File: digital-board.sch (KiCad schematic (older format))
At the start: 200 parts, among them IC1 ATMEGA6450-A, J1 CONN_20X2, Q1 2N3904, Q10 2N3904, Q11 2N3904, Q12 2N3904, Q13 2N3904, Q14 2N3904, Q15 2N3904, Q16 2N3904, Q2 2N3904, Q3 2N3904, Q4 2N3904, Q5 2N3904, Q6 2N3904, Q7 2N3904, Q8 2N3904, Q9 2N3904, SW15 TACT_SWITCH, SW16 TACT_SWITCH, SW17 TACT_SWITCH, SW18 TACT_SWITCH, SW19 TACT_SWITCH, SW20 TACT_SWITCH, SW21 TACT_SWITCH, SW22 TACT_SWITCH, SW23 TACT_SWITCH, U1 DG419, U10 74LVC1G32, U2 74HC4067, U3 R-78E5.0-1.0, U4 74HC4067, U5 74LS573, U6 74LS573, U7 74LVC2G04, U8 74LS573, U9 74LS573, X1 MIDI OUT, X2 MIDI IN, X3 MIDI THRU

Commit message: commit
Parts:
- removed U8, U9: 74LS573, symbol 74LS573
- added U?: 74AC273, symbol 74AC273
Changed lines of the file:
@@
 $EndComp
 $Comp
-L 74LS573 U9
-U 1 1 5458825E
-P 18600 16650
-F 0 "U9" H 18750 17250 60  0000 C CNN
-F 1 "74LS573" H 18850 16050 60  0000 C CNN
-F 2 "" H 18600 16650 60  0000 C CNN
-F 3 "" H 18600 16650 60  0000 C CNN
-	1    18600 16650
-	1    0    0    -1
-$EndComp
-$Comp
 L C_US C14
 U 1 1 54588264
@@
 LFO SYNC LED DRIVEN BY LFO OUTPUT\nLED DRIVER FROM YUSYNTH VCO\nTESTED BY BREADBOARD
 $Comp
-L 74LS573 U8
-U 1 1 545882D7
-P 16250 11350
-F 0 "U8" H 16400 11950 60  0000 C CNN
-F 1 "74LS573" H 16500 10750 60  0000 C CNN
-F 2 "" H 16250 11350 60  0000 C CNN
-F 3 "" H 16250 11350 60  0000 C CNN
-	1    16250 11350
-	1    0    0    -1
-$EndComp
-$Comp
 L C_US C13
 U 1 1 545882DD
@@
 Wire Wire Line
 	19500 20200 19750 20200
-Wire Notes Line
-	30000 2800 30000 5800
-Wire Notes Line
-	30000 5800 29550 5800
-Wire Notes Line
-	29550 5800 29550 3500
-Wire Notes Line
-	29550 3500 31600 3500
-Wire Notes Line
-	31600 3500 31600 9100
-Wire Notes Line
-	31600 9100 32300 9100
-Wire Notes Line
-	32300 9100 32300 6850
-Wire Notes Line
-	32300 6850 30150 6850
-Wire Notes Line
-	30150 6850 30150 11000
+$Comp
+L 74AC273 U?
+U 1 1 54A8D023
+P 30350 8100
+F 0 "U?" H 30000 8700 60  0000 C CNN
+F 1 "74AC273" H 30575 7500 60  0000 C CNN
+F 2 "" H 30350 8100 60  0000 C CNN
+F 3 "" H 30350 8100 60  0000 C CNN
+	1    30350 8100
+	1    0    0    -1
+$EndComp
 $EndSCHEMATC

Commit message: working on 74AC595 LED arrays
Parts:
- removed C14, C15: 0.1µ, ~, symbol C_US
- removed Q10, Q11, Q12, Q13, Q14, Q15, Q2, Q3, Q4, Q5, Q6, Q7, Q8, Q9: 2N3904, ~, symbol NPN
- removed U?: 74AC273, symbol 74AC273
- added C? (x4): 0.1µ, ~, symbol C_US
- added R? (x3): 1K, ~, symbol R_US
- added R?: 10K, ~, symbol R_US
- added R? (x33): 470, ~, symbol R_US
- added U? (x5): 74AC595, symbol 74AC595
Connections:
- net labels added: ARP_SYNC, LED_LATCH, SPI_MISO, SPI_MOSI, SPI_RESET, SPI_SCK
- net labels removed: LED ANODE LATCH, LED CATHODE LATCH, SW ROW 3
- wire segments 813 -> 858
- no-connect marks 17 -> 16
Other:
- note added: "LED INTERFACE"
- note added: "SWITCH INTERFACE"
- note removed: "LED MATRIX"
- note removed: "SWITCH MATRIX"
- moved on the sheet: C13, C17, D10, D11, D12, D13, D14, D15, D16, D17, D18, D19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

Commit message: led and switch interfaces
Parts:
- removed D10, D11, D12, D13, D14, D15, D16, D17, D18, D19, D2, D20, D21, D22, D23, D3, D4, D5, D6, D7, D8, D9: 1N4148, ~, symbol DIODE
- added C? (x3): 0.1µ, ~, symbol C_US
- added R? (x23): 10K, ~, symbol R_US
- added TP? (x2): CONN_1, symbol CONN_1
- added U? (x3): 74HC165, symbol 74HC165
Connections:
- net +5V: now also ISW1.1, ISW1.2, ISW10.1, ISW10.2, ISW11.1, ISW11.2, ISW12.1, ISW12.2, ISW13.1, ISW13.2, ISW14.1, ISW14.2, ISW2.1, ISW2.2, ISW3.1, ISW3.2, ISW4.1, ISW4.2, ISW5.1, ISW5.2, ISW6.1, ISW6.2, ISW7.1, ISW7.2, ISW8.1, ISW8.2, ISW9.1, ISW9.2, SW15.1, SW15.2, SW16.1, SW16.2, SW17.1, SW17.2, SW18.1, SW18.2, SW19.1, SW19.2, SW20.1, SW20.2, SW21.1, SW21.2, SW22.1, SW22.2, C?.1, C?.1, C?.1, R?.1, U?.16 (VCC), U?.16 (VCC), U?.16 (VCC)
- net GND: now also C?.2, C?.2, C?.2, R?.1, R?.1, R?.1, R?.1, R?.1, R?.1, R?.1, R?.1, R?.1, R?.1, R?.1, R?.1, R?.1, R?.1, R?.1, R?.1, R?.1, R?.1, R?.1, R?.1, R?.1, R?.1, U?.15 (~CE), U?.15 (~CE), U?.5 (D6), U?.6 (D7), U?.8 (GND), U?.8 (GND), U?.8 (GND)
- net SPI_MISO: now also TP?.1, U?.9 (Q7)
- net SPI_RESET: now also R?.2, U?.15 (~CE)
- net SPI_SCK: now also U?.2 (SCK), U?.2 (SCK), U?.2 (SCK)
- net at U?.9 (Q7S): now also TP?.1
- removed net SW ROW 0: ISW1.3, ISW1.4, ISW2.3, ISW2.4, ISW3.3, ISW3.4, ISW4.3, ISW4.4, ISW5.3, ISW5.4, ISW6.3, ISW6.4, ISW7.3, ISW7.4, ISW8.3, ISW8.4
- removed net SW ROW 1: ISW10.3, ISW10.4, ISW11.3, ISW11.4, ISW12.3, ISW12.4, ISW13.3, ISW13.4, ISW14.3, ISW14.4, ISW9.3, ISW9.4, SW15.3, SW15.4, SW16.3, SW16.4
- removed net SW ROW 2: SW17.3, SW17.4, SW18.3, SW18.4, SW19.3, SW19.4, SW20.3, SW20.4, SW21.3, SW21.4, SW22.3, SW22.4
- new net: ISW1.3, ISW1.4, R?.2, U?.11 (D0)
- new net: ISW2.3, ISW2.4, R?.2, U?.12 (D1)
- new net: ISW3.3, ISW3.4, R?.2, U?.13 (D2)
- new net: ISW4.3, ISW4.4, R?.2, U?.14 (D3)
- new net: ISW5.3, ISW5.4, R?.2, U?.3 (D4)
- new net: ISW6.3, ISW6.4, R?.2, U?.4 (D5)
- new net: ISW7.3, ISW7.4, R?.2, U?.5 (D6)
- new net: ISW8.3, ISW8.4, R?.2, U?.11 (D0)
- new net: ISW9.3, ISW9.4, R?.2, U?.12 (D1)
- new net: ISW10.3, ISW10.4, R?.2, U?.13 (D2)
- new net: ISW11.3, ISW11.4, R?.2, U?.14 (D3)
- new net: ISW12.3, ISW12.4, R?.2, U?.6 (D7)
- new net: R?.2, SW20.3, SW20.4, U?.5 (D6)
- new net: R?.2, SW19.3, SW19.4, U?.14 (D3)
- new net: R?.2, SW18.3, SW18.4, U?.13 (D2)
- new net: R?.2, SW21.3, SW21.4, U?.3 (D4)
- new net: R?.2, SW15.3, SW15.4, U?.6 (D7)
- new net: R?.2, SW16.3, SW16.4, U?.11 (D0)
- new net: R?.2, SW17.3, SW17.4, U?.12 (D1)
- new net: ISW13.3, ISW13.4, R?.2, U?.4 (D5)
- new net: R?.2, SW22.3, SW22.4, U?.4 (D5)
- new net: ISW14.3, ISW14.4, R?.2, U?.3 (D4)
- new net: U?.10 (SER), U?.9 (Q7) (x2)
- new net SWITCH_LATCH: U?.1 (~PL), U?.1 (~PL), U?.1 (~PL)
- no-connect marks 16 -> 19
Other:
- moved on the sheet: C17, ISW10A, ISW11A, ISW12A, ISW13A, ISW13B, ISW14A, ISW14B, ISW1A, ISW2A, ISW3A, ISW4A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

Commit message: laying out board with led rework changes
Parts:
- added R92: 10K, ~, symbol R_US
- added TP6, TP7, TP8: CONN_1, symbol CONN_1
- gave numbers to parts that had none: 77
- renumbered Q16 to Q2, TP3 to TP1, TP8 to TP11, TP1 to TP12, TP2 to TP13, TP4 to TP2, TP5 to TP3, TP6 to TP4, TP7 to TP5
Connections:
- net ANALOG SW LATCH: now also IC1.68 (PC6); no longer IC1.19 ((PCINT8/~SS~)PB0)
- net ARP_SYNC: now also IC1.26 ((PCINT15/OC2A)PB7); no longer IC1.49 (PD6)
- net DAC MUX EN0: now also IC1.53 (PC0); no longer IC1.43 ((ICP1)PD0)
- net DAC MUX EN1: now also IC1.54 (PC1); no longer IC1.44 ((INT0)PD1)
- net DAC MUX EN2: now also IC1.55 (PC2); no longer IC1.45 (PD2)
- net DAC MUX EN3: now also IC1.56 (PC3); no longer IC1.46 (PD3)
- net DISP ANODE LATCH: now also IC1.58 (PC5); no longer IC1.48 (PD5)
- net DISP CATHODE LATCH: now also IC1.57 (PC4); no longer IC1.47 (PD4)
- net GND: now also LED13.2 (K), R92.1
- net LED_LATCH: now also IC1.25 ((PCINT14/OC1B)PB6); no longer IC1.50 (PD7)
- net SWITCH_LATCH: now also IC1.24 ((PCINT13/OC1A)PB5)
- net at TP1.1: now also IC1.43 ((ICP1)PD0); no longer IC1.5 ((PCINT3/AIN1)PE3)
- net at TP2.1: now also IC1.44 ((INT0)PD1); no longer IC1.6 ((PCINT4/USCK/SCL)PE4)
- net at TP3.1: now also IC1.45 (PD2); no longer IC1.7 ((PCINT5/DI/SDA)PE5)
- net at TP4.1: now also IC1.46 (PD3); no longer IC1.8 ((PCINT6/DO)PE6)
- net at TP5.1: now also IC1.47 (PD4); no longer IC1.9 ((PCINT7/CLKO)PE7)
- net at SW23.1, SW23.2, U10.1: now also R92.2
- net SPI_RESET renamed ~SPI_EN
- net ~SPI_EN: now also IC1.19 ((PCINT8/~SS~)PB0)
- new net: IC1.48 (PD5), TP6.1
- new net: IC1.49 (PD6), TP7.1
- new net: IC1.50 (PD7), TP8.1
- no-connect marks 19 -> 25
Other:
- moved on the sheet: C17, R46, R47, R48, TP1, TP2, TP3, TP4, TP5

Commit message: led driver layout
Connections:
- net at ISW1.6 (A): now also R24.1; no longer R22.1
- net at ISW2.6 (A): now also R25.1; no longer R23.1
- net at ISW3.6 (A): now also R22.1; no longer R24.1
- net at ISW4.6 (A): now also R23.1; no longer R25.1
- net at R80.2: now also U15.1 (Q1); no longer U15.15 (Q0)
- net at R81.2: now also U15.2 (Q2); no longer U15.1 (Q1)
- net at R83.2: now also U15.15 (Q0); no longer U15.2 (Q2)
- net at R76.2: now also U13.7 (Q7); no longer U13.6 (Q6)
- net at R78.2: now also U13.6 (Q6); no longer U13.7 (Q7)
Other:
- moved on the sheet: ISW1B, ISW2B, ISW3B, ISW4B, LED25, LED26, LED3, LED4, LED5, R76, R78, R80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

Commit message: LED array layout
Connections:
- net at R32.2: now also U8.2 (Q2); no longer U8.15 (Q0)
- net at R35.2: now also U8.5 (Q5); no longer U8.2 (Q2)
- net at R38.2: now also U8.4 (Q4); no longer U8.3 (Q3)
- net at R39.2: now also U8.3 (Q3); no longer U8.4 (Q4)
- net at R42.2: now also U8.15 (Q0); no longer U8.5 (Q5)
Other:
- moved on the sheet: ISW12B, ISW9B, LED28, LED29, LED30, R32, R35, R38, R39, R42
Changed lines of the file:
@@
 L TL1240 ISW12
 U 2 1 54588138
-P 18650 950
-F 0 "ISW12" H 18650 1100 50  0000 C CNN
-F 1 "TL1240" H 18650 775 50  0000 C CNN
-F 2 "~" H 18650 800 60  0000 C CNN
-F 3 "~" H 18650 800 60  0000 C CNN
-	2    18650 950
+P 18650 1850
+F 0 "ISW12" H 18650 2000 50  0000 C CNN
+F 1 "TL1240" H 18650 1675 50  0000 C CNN
+F 2 "~" H 18650 1700 60  0000 C CNN
+F 3 "~" H 18650 1700 60  0000 C CNN
+	2    18650 1850
 	1    0    0    -1
 $EndComp
@@
 L TL1240 ISW9
 U 2 1 54588150
-P 18650 3200
-F 0 "ISW9" H 18650 3350 50  0000 C CNN
-F 1 "TL1240" H 18650 3025 50  0000 C CNN
-F 2 "~" H 18650 3050 60  0000 C CNN
-F 3 "~" H 18650 3050 60  0000 C CNN
-	2    18650 3200
+P 18600 950
+F 0 "ISW9" H 18600 1100 50  0000 C CNN
+F 1 "TL1240" H 18600 775 50  0000 C CNN
+F 2 "~" H 18600 800 60  0000 C CNN
+F 3 "~" H 18600 800 60  0000 C CNN
+	2    18600 950
 	1    0    0    -1
 $EndComp
@@
 L LED LED28
 U 1 1 5498F098
-P 18600 1850
-F 0 "LED28" H 18600 1950 50  0000 C CNN
-F 1 "LED" H 18600 1750 50  0000 C CNN
-F 2 "" H 18600 1850 60  0000 C CNN
-F 3 "" H 18600 1850 60  0000 C CNN
-	1    18600 1850
+P 18600 3200
+F 0 "LED28" H 18600 3300 50  0000 C CNN
+F 1 "LED" H 18600 3100 50  0000 C CNN
+F 2 "" H 18600 3200 60  0000 C CNN
+F 3 "" H 18600 3200 60  0000 C CNN
+	1    18600 3200
 	1    0    0    -1
 $EndComp
@@
 L LED LED29
 U 1 1 5498F189
-P 18600 2300
-F 0 "LED29" H 18600 2400 50  0000 C CNN
-F 1 "LED" H 18600 2200 50  0000 C CNN
-F 2 "" H 18600 2300 60  0000 C CNN
-F 3 "" H 18600 2300 60  0000 C CNN
-	1    18600 2300
-	1    0    0    -1
-$EndComp
-$Comp
-L LED LED30
-U 1 1 5498F667
 P 18600 2750
-F 0 "LED30" H 18600 2850 50  0000 C CNN
+F 0 "LED29" H 18600 2850 50  0000 C CNN
 F 1 "LED" H 18600 2650 50  0000 C CNN
 F 2 "" H 18600 2750 60  0000 C CNN
@@
 $EndComp
 $Comp
+L LED LED30
+U 1 1 5498F667
+P 18600 2300
+F 0 "LED30" H 18600 2400 50  0000 C CNN
+F 1 "LED" H 18600 2200 50  0000 C CNN
+F 2 "" H 18600 2300 60  0000 C CNN
+F 3 "" H 18600 2300 60  0000 C CNN
+	1    18600 2300
+	1    0    0    -1
+$EndComp
+$Comp
 L POT_US VR1
 U 1 1 54999BFB
@@
 L R_US R32
 U 1 1 54AFD600
-P 18050 950
-F 0 "R32" V 18100 1100 50  0000 C CNN
-F 1 "470" V 17970 950 50  0000 C CNN
-F 2 "~" H 18050 950 60  0000 C CNN
-F 3 "~" H 18050 950 60  0000 C CNN
-	1    18050 950
+P 18050 1850
+F 0 "R32" V 18100 2000 50  0000 C CNN
+F 1 "470" V 17970 1850 50  0000 C CNN
+F 2 "~" H 18050 1850 60  0000 C CNN
+F 3 "~" H 18050 1850 60  0000 C CNN
+	1    18050 1850
 	0    1    1    0
 $EndComp
@@
 L R_US R35
 U 1 1 54AFD60C
-P 18050 1850
-F 0 "R35" V 18100 2000 50  0000 C CNN
-F 1 "470" V 17970 1850 50  0000 C CNN
-F 2 "~" H 18050 1850 60  0000 C CNN
-F 3 "~" H 18050 1850 60  0000 C CNN
-	1    18050 1850
+P 18050 3200
+F 0 "R35" V 18100 3350 50  0000 C CNN
+F 1 "470" V 17970 3200 50  0000 C CNN
+F 2 "~" H 18050 3200 60  0000 C CNN
+F 3 "~" H 18050 3200 60  0000 C CNN
+	1    18050 3200
 	0    1    1    0
 $EndComp
@@
 L R_US R38
 U 1 1 54AFD612
-P 18050 2300
-F 0 "R38" V 18100 2450 50  0000 C CNN
-F 1 "470" V 17970 2300 50  0000 C CNN
-F 2 "~" H 18050 2300 60  0000 C CNN
-F 3 "~" H 18050 2300 60  0000 C CNN
-	1    18050 2300
-	0    1    1    0
-$EndComp
-$Comp
-L R_US R39
-U 1 1 54AFD618
 P 18050 2750
-F 0 "R39" V 18100 2900 50  0000 C CNN
+F 0 "R38" V 18100 2900 50  0000 C CNN
 F 1 "470" V 17970 2750 50  0000 C CNN
 F 2 "~" H 18050 2750 60  0000 C CNN
@@
 $EndComp
 $Comp
+L R_US R39
+U 1 1 54AFD618
+P 18050 2300
+F 0 "R39" V 18100 2450 50  0000 C CNN
+F 1 "470" V 17970 2300 50  0000 C CNN
+F 2 "~" H 18050 2300 60  0000 C CNN
+F 3 "~" H 18050 2300 60  0000 C CNN
+	1    18050 2300
+	0    1    1    0
+$EndComp
+$Comp
 L R_US R42
 U 1 1 54AFD61E
-P 18050 3200
-F 0 "R42" V 18100 3350 50  0000 C CNN
-F 1 "470" V 17970 3200 50  0000 C CNN
-F 2 "~" H 18050 3200 60  0000 C CNN
-F 3 "~" H 18050 3200 60  0000 C CNN
-	1    18050 3200
+P 18000 950
+F 0 "R42" V 18050 1100 50  0000 C CNN
+F 1 "470" V 17920 950 50  0000 C CNN
+F 2 "~" H 18000 950 60  0000 C CNN
+F 3 "~" H 18000 950 60  0000 C CNN
+	1    18000 950
 	0    1    1    0
 $EndComp
@@
 	16300 3400 16300 3500
 Wire Wire Line
-	17850 950  17150 950
+	17150 950  17800 950
 Wire Wire Line
 	17150 950  17150 2100
@@
 	18800 2300 19150 2300
 Connection ~ 19150 2300
-Wire Wire Line
-	18800 1850 19150 1850
 Connection ~ 19150 1850
 Wire Wire Line
@@
 	19050 4100 19150 4100
 Wire Wire Line
-	19050 3200 19150 3200
+	18800 3200 19150 3200
 Wire Wire Line
-	19050 950  19150 950
+	19000 950  19150 950
 Wire Wire Line
 	18250 1400 18400 1400
 Wire Wire Line
-	18250 1850 18400 1850
-Wire Wire Line
-	18250 2300 18400 2300
+	18250 3200 18400 3200
 Wire Wire Line
 	18250 2750 18400 2750
 Wire Wire Line
+	18250 2300 18400 2300
+Wire Wire Line
 	17200 20700 17200 21000
 Wire Wire Line
@@
 Wire Wire Line
 	3500 10250 3500 10450
+Wire Wire Line
+	19050 1850 19150 1850
 $EndSCHEMATC

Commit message: layout of switch interface
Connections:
- net GND: now also U11.11 (D0), U11.12 (D1); no longer U11.5 (D6), U11.6 (D7)
- net at ISW1.3, ISW1.4: now also R74.2, U14.13 (D2); no longer R68.2, U14.11 (D0)
- net at ISW3.3, ISW3.4: now also R68.2, U14.11 (D0); no longer R74.2, U14.13 (D2)
- net at ISW4.3, ISW4.4: now also R88.2, U14.6 (D7); no longer R77.2, U14.14 (D3)
- net at ISW8.3, ISW8.4: now also R41.2, U11.14 (D3); no longer R37.2, U11.11 (D0)
- net at ISW9.3, ISW9.4: now also R37.2, U11.13 (D2); no longer R41.2, U11.12 (D1)
- net at ISW10.3, ISW10.4: now also R60.2, U11.6 (D7); no longer R45.2, U11.13 (D2)
- net at ISW11.3, ISW11.4: now also R56.2, U11.5 (D6); no longer R51.2, U11.14 (D3)
- net at ISW12.3, ISW12.4: now also R63.2, U9.5 (D6); no longer R65.2, U9.6 (D7)
- net at SW20.3, SW20.4: now also R59.2, U9.4 (D5); no longer R63.2, U9.5 (D6)
- net at SW19.3, SW19.4: now also R65.2, U9.6 (D7); no longer R50.2, U9.14 (D3)
- net at SW18.3, SW18.4: now also R40.2, U9.12 (D1); no longer R44.2, U9.13 (D2)
- net at SW21.3, SW21.4, U11.3 (D4): now also R45.2; no longer R56.2
- net at SW15.3, SW15.4: now also R77.2, U14.14 (D3); no longer R88.2, U14.6 (D7)
- net at SW16.3, SW16.4: now also R50.2, U9.14 (D3); no longer R36.2, U9.11 (D0)
- net at SW17.3, SW17.4: now also R44.2, U9.13 (D2); no longer R40.2, U9.12 (D1)
- net at ISW13.3, ISW13.4: now also R55.2, U9.3 (D4); no longer R59.2, U9.4 (D5)
- net at SW22.3, SW22.4, U11.4 (D5): now also R51.2; no longer R60.2
- net at ISW14.3, ISW14.4: now also R36.2, U9.11 (D0); no longer R55.2, U9.3 (D4)
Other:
- note added: "THIS ENABLE IS OF QUESTIONABLE USE\nTO STOP LEDS\nFROM BLINKING\nDURING MCU BOOT\nNEED EN/PULLUP\nON ALL 595s"
- moved on the sheet: ISW10A, ISW11A, ISW12A, ISW13A, ISW14A, ISW1A, ISW3A, ISW4A, ISW8A, ISW9A, R37, R41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

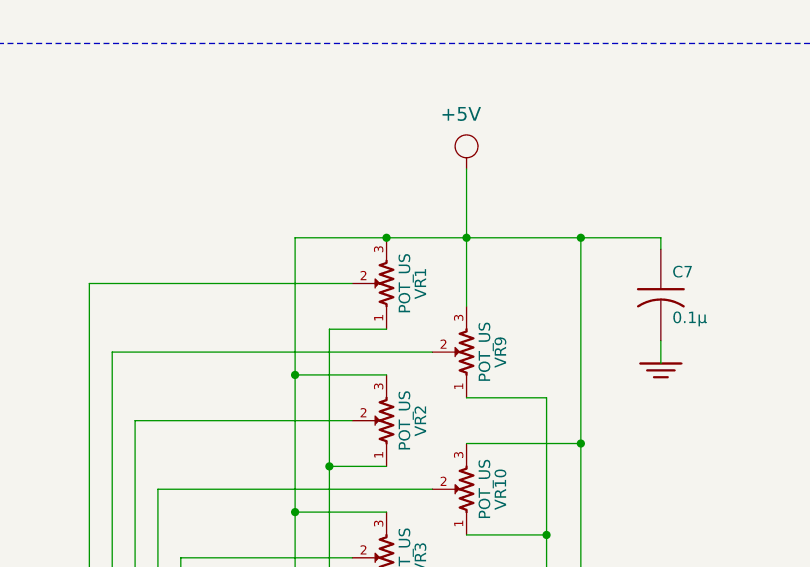
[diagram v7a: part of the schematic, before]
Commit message: laying out POT multiplexors
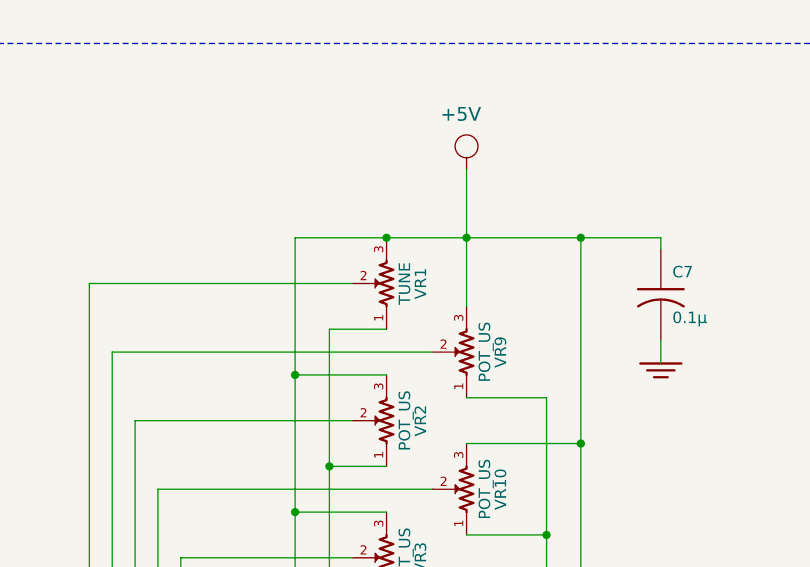
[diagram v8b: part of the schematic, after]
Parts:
- VR1: value POT_US -> TUNE
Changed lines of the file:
@@
 P 5950 15700
 F 0 "VR1" H 5950 15550 50  0000 C CNN
-F 1 "POT_US" H 5950 15620 50  0000 C CNN
+F 1 "TUNE" H 5950 15620 50  0000 C CNN
 F 2 "" H 5950 15700 60  0000 C CNN
 F 3 "" H 5950 15700 60  0000 C CNN
@@
 $EndComp
 $Comp
-L +5V #PWR0113
+L +5V #PWR0112
 U 1 1 54C668DF
 P 25550 4750
-F 0 "#PWR0113" H 25550 4850 30  0001 C CNN
+F 0 "#PWR0112" H 25550 4850 30  0001 C CNN
 F 1 "+5V" H 25525 5025 60  0000 C TNN
 F 2 "~" H 25550 4750 60  0000 C CNN
@@
 $EndComp
 $Comp
-L +5V #PWR0114
+L +5V #PWR0113
 U 1 1 54C71070
 P 29550 1550
-F 0 "#PWR0114" H 29550 1650 30  0001 C CNN
+F 0 "#PWR0113" H 29550 1650 30  0001 C CNN
 F 1 "+5V" H 29525 1825 60  0000 C TNN
 F 2 "~" H 29550 1550 60  0000 C CNN
@@
 $EndComp
 $Comp
-L GND_E #PWR0115
+L GND_E #PWR0114
 U 1 1 54CC7E9A
 P 22900 18400
-F 0 "#PWR0115" V 22900 18400 30  0001 C CNN
+F 0 "#PWR0114" V 22900 18400 30  0001 C CNN
 F 1 "GND_E" H 22900 18330 30  0001 C CNN
 F 2 "~" H 22900 18400 60  0000 C CNN
